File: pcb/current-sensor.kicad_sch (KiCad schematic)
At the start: 37 parts, among them U1 SS39ET, U2 TLV9064, U3 SS39ET

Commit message: Fixed part values; added name to scripts
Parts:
- C1, C10, C4, C5: LCSC C106217 -> C106857; MPN CC0603KRX7R8BB223 -> CC0603KRX7R8BB224; Mouser (none) -> 603-CC603KRX7R8BB224
- C11: Digikey (none) -> 1276-1870-2-ND; Mouser (none) -> 187-CL10A106MO8NQNC
- C3, C8, C9: Digikey (none) -> 1276-1005-2-ND; Mouser (none) -> 187-CL10B104KO8NNNC
- C7: Digikey (none) -> 311-4098-2-ND; Mouser (none) -> 603-CC603KRX7R9BB202
- R1, R5: Digikey (none) -> CR0603-JW-304ELFTR-ND; Mouser (none) -> 652-CR0603JW-304ELF
- R10, R11, R2, R8: Digikey (none) -> CR0603-JW-104ELFTR-ND; Mouser (none) -> 652-CR0603-JW-104ELF
- R3, R4, R9: Digikey (none) -> 541-4.99KHTR-ND; Mouser (none) -> 71-CRCW0603-4.99K-E3
- R6: Digikey (none) -> CR0603-JW-106ELFTR-ND; Mouser (none) -> 652-CR0603JW-106ELF
- R7: Digikey (none) -> CR0603-JW-105ELFTR-ND; Mouser (none) -> 652-CR0603JW-105ELF
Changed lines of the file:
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@@
 			)
 		)
+		(property "Digikey" "1276-1005-2-ND"
+			(at 128.27 55.88 0)
+			(effects
+				(font
+					(size 1.27 1.27)
+				)
+				(hide yes)
+			)
+		)
+		(property "Mouser" "187-CL10B104KO8NNNC"
+			(at 128.27 55.88 0)
+			(effects
+				(font
+					(size 1.27 1.27)
+				)
+				(hide yes)
+			)
+		)
 		(pin "1"
 		)
@@
 			)
 		)
-		(property "Digikey" ""
+		(property "Digikey" "CR0603-JW-104ELFTR-ND"
 			(at 38.1 163.83 90)
 			(effects
@@
 			)
 		)
-		(property "Mouser" ""
+		(property "Mouser" "652-CR0603-JW-104ELF"
 			(at 38.1 163.83 90)
 			(effects
@@
 			)
 		)
-		(property "MPN" "CC0603KRX7R8BB223"
+		(property "MPN" "CC0603KRX7R8BB224"
 			(at 162.56 71.12 0)
 			(effects
@@
 			)
 		)
-		(property "Mouser" ""
+		(property "Mouser" "603-CC603KRX7R8BB224"
 			(at 162.56 71.12 90)
 			(effects
@@
 			)
 		)
-		(property "LCSC" "C106217"
+		(property "LCSC" "C106857"
 			(at 162.56 71.12 0)
 			(effects
@@
 			)
 		)
+		(property "Digikey" "1276-1005-2-ND"
+			(at 107.95 154.94 0)
+			(effects
+				(font
+					(size 1.27 1.27)
+				)
+				(hide yes)
+			)
+		)
+		(property "Mouser" "187-CL10B104KO8NNNC"
+			(at 107.95 154.94 0)
+			(effects
+				(font
+					(size 1.27 1.27)
+				)
+				(hide yes)
+			)
+		)
 		(pin "1"
 		)
@@
 			)
 		)
-		(property "Digikey" ""
+		(property "Digikey" "541-4.99KHTR-ND"
 			(at 86.36 53.34 90)
 			(effects
@@
 			)
 		)
-		(property "Mouser" ""
+		(property "Mouser" "71-CRCW0603-4.99K-E3"
 			(at 86.36 53.34 90)
 			(effects
@@
 			)
 		)
-		(property "MPN" "CC0603KRX7R8BB223"
+		(property "MPN" "CC0603KRX7R8BB224"
 			(at 194.31 77.47 0)
 			(effects
@@
 			)
 		)
-		(property "Mouser" ""
+		(property "Mouser" "603-CC603KRX7R8BB224"
 			(at 194.31 77.47 90)
 			(effects
@@
 			)
 		)
-		(property "LCSC" "C106217"
+		(property "LCSC" "C106857"
 			(at 194.31 77.47 0)
 			(effects
@@
 			)
 		)
-		(property "Digikey" ""
+		(property "Digikey" "CR0603-JW-104ELFTR-ND"
 			(at 38.1 146.05 90)
 			(effects
@@
 			)
 		)
-		(property "Mouser" ""
+		(property "Mouser" "652-CR0603-JW-104ELF"
 			(at 38.1 146.05 90)
 			(effects
@@
 			)
 		)
-		(property "Digikey" ""
+		(property "Digikey" "541-4.99KHTR-ND"
 			(at 85.09 81.28 90)
 			(effects
@@
 			)
 		)
-		(property "Mouser" ""
+		(property "Mouser" "71-CRCW0603-4.99K-E3"
 			(at 85.09 81.28 90)
 			(effects
@@
 			)
 		)
-		(property "Digikey" ""
+		(property "Digikey" "CR0603-JW-106ELFTR-ND"
 			(at 199.39 77.47 90)
 			(effects
@@
 			)
 		)
-		(property "Mouser" ""
+		(property "Mouser" "652-CR0603JW-106ELF"
 			(at 199.39 77.47 90)
 			(effects
@@
 			)
 		)
-		(property "Mouser" ""
+		(property "Mouser" "603-CC603KRX7R9BB202"
 			(at 111.76 81.28 0)
 			(effects
@@
 			)
 		)
-		(property "Digikey" ""
+		(property "Digikey" "311-4098-2-ND"
 			(at 111.76 81.28 0)
 			(effects
@@
 			)
 		)
+		(property "Digikey" "1276-1005-2-ND"
+			(at 118.11 154.94 0)
+			(effects
+				(font
+					(size 1.27 1.27)
+				)
+				(hide yes)
+			)
+		)
+		(property "Mouser" "187-CL10B104KO8NNNC"
+			(at 118.11 154.94 0)
+			(effects
+				(font
+					(size 1.27 1.27)
+				)
+				(hide yes)
+			)
+		)
 		(pin "1"
 		)
@@
 			)
 		)
-		(property "Mouser" ""
+		(property "Mouser" "187-CL10A106MO8NQNC"
 			(at 30.48 163.83 0)
 			(effects
@@
 			)
 		)
-		(property "Digikey" ""
+		(property "Digikey" "1276-1870-2-ND"
 			(at 30.48 163.83 0)
 			(effects
@@
 			)
 		)
-		(property "Digikey" ""
+		(property "Digikey" "CR0603-JW-304ELFTR-ND"
 			(at 111.76 74.93 90)
 			(effects
@@
 			)
 		)
-		(property "Mouser" ""
+		(property "Mouser" "652-CR0603JW-304ELF"
 			(at 111.76 74.93 90)
 			(effects
@@
 			)
 		)
-		(property "Digikey" ""
+		(property "Digikey" "CR0603-JW-104ELFTR-ND"
 			(at 148.59 80.01 90)
 			(effects
@@
 			)
 		)
-		(property "Mouser" ""
+		(property "Mouser" "652-CR0603-JW-104ELF"
 			(at 148.59 80.01 90)
 			(effects
@@
 			)
 		)
-		(property "Digikey" ""
+		(property "Digikey" "CR0603-JW-304ELFTR-ND"
 			(at 85.09 35.56 90)
 			(effects
@@
 			)
 		)
-		(property "Mouser" ""
+		(property "Mouser" "652-CR0603JW-304ELF"
 			(at 85.09 35.56 90)
 			(effects
@@
 			)
 		)
-		(property "MPN" "CC0603KRX7R8BB223"
+		(property "MPN" "CC0603KRX7R8BB224"
 			(at 146.05 154.94 0)
 			(effects
@@
 			)
 		)
-		(property "Mouser" ""
+		(property "Mouser" "603-CC603KRX7R8BB224"
 			(at 146.05 154.94 90)
 			(effects
@@
 			)
 		)
-		(property "LCSC" "C106217"
+		(property "LCSC" "C106857"
 			(at 146.05 154.94 0)
 			(effects
@@
 			)
 		)
-		(property "Digikey" ""
+		(property "Digikey" "CR0603-JW-105ELFTR-ND"
 			(at 140.97 80.01 90)
 			(effects
@@
 			)
 		)
-		(property "Mouser" ""
+		(property "Mouser" "652-CR0603JW-105ELF"
 			(at 140.97 80.01 90)
 			(effects
@@
 			)
 		)
-		(property "Digikey" ""
+		(property "Digikey" "541-4.99KHTR-ND"
 			(at 187.96 58.42 90)
 			(effects
@@
 			)
 		)
-		(property "Mouser" ""
+		(property "Mouser" "71-CRCW0603-4.99K-E3"
 			(at 187.96 58.42 90)
 			(effects
@@
 			)
 		)
-		(property "MPN" "CC0603KRX7R8BB223"
+		(property "MPN" "CC0603KRX7R8BB224"
 			(at 208.28 41.91 0)
 			(effects
@@
 			)
 		)
-		(property "Mouser" ""
+		(property "Mouser" "603-CC603KRX7R8BB224"
 			(at 208.28 41.91 90)
 			(effects
@@
 			)
 		)
-		(property "LCSC" "C106217"
+		(property "LCSC" "C106857"
 			(at 208.28 41.91 0)
 			(effects
@@
 			)
 		)
-		(property "Digikey" ""
+		(property "Digikey" "CR0603-JW-104ELFTR-ND"
 			(at 201.93 35.56 90)
 			(effects
@@
 			)
 		)
-		(property "Mouser" ""
+		(property "Mouser" "652-CR0603-JW-104ELF"
 			(at 201.93 35.56 90)
 			(effects

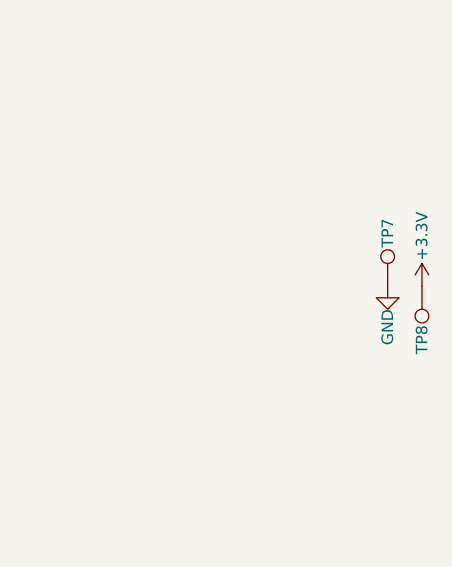
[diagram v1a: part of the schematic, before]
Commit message: Removed CSV bom file; moved logos to symbols
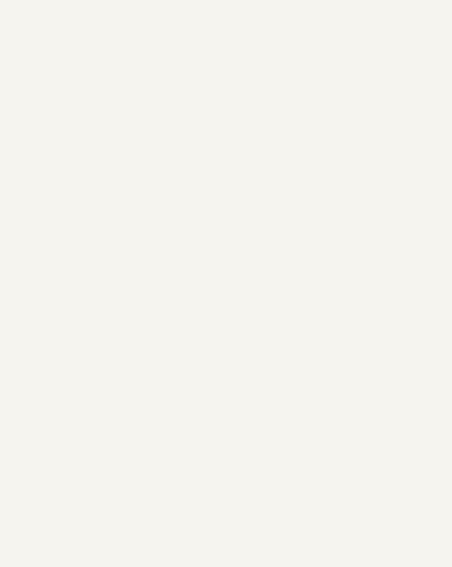
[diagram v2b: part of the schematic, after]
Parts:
- removed TP7, TP8: ~, CRGM Mechanical:TestPoint_Pad_D1.0mm, symbol Connector:TestPoint
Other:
- title: Current Detector -> Current Sensor

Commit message: Updated to all CRGM footprints
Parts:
- D1, D2: footprint Diode_SMD:D_SOD-323F -> CRGM Passive:D_SOD-323F
- U1, U3: footprint Package_TO_SOT_SMD:SOT-23 -> CRGM Passive:SOT-23
- U2: footprint Package_SO:SOIC-14_3.9x8.7mm_P1.27mm -> CRG Makes:SOIC-14_3.9x8.7mm_P1.27mm
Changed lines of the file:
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@@
 			)
 		)
-		(property "Footprint" "Package_SO:SOIC-14_3.9x8.7mm_P1.27mm"
+		(property "Footprint" "CRG Makes:SOIC-14_3.9x8.7mm_P1.27mm"
 			(at 162.56 55.88 0)
 			(effects
@@
 			)
 		)
-		(property "Footprint" "Package_TO_SOT_SMD:SOT-23"
+		(property "Footprint" "CRGM Passive:SOT-23"
 			(at 58.42 61.976 0)
 			(effects
@@
 			)
 		)
-		(property "Footprint" "Diode_SMD:D_SOD-323F"
+		(property "Footprint" "CRGM Passive:D_SOD-323F"
 			(at 130.175 80.01 0)
 			(effects
@@
 			)
 		)
-		(property "Footprint" "Package_SO:SOIC-14_3.9x8.7mm_P1.27mm"
+		(property "Footprint" "CRG Makes:SOIC-14_3.9x8.7mm_P1.27mm"
 			(at 55.88 153.67 0)
 			(effects
@@
 			)
 		)
-		(property "Footprint" "Diode_SMD:D_SOD-323F"
+		(property "Footprint" "CRGM Passive:D_SOD-323F"
 			(at 176.53 53.975 0)
 			(effects
@@
 			)
 		)
-		(property "Footprint" "Package_SO:SOIC-14_3.9x8.7mm_P1.27mm"
+		(property "Footprint" "CRG Makes:SOIC-14_3.9x8.7mm_P1.27mm"
 			(at 212.09 58.42 0)
 			(effects
@@
 			)
 		)
-		(property "Footprint" "Package_TO_SOT_SMD:SOT-23"
+		(property "Footprint" "CRGM Passive:SOT-23"
 			(at 58.42 89.916 0)
 			(effects
@@
 			)
 		)
-		(property "Footprint" "Package_SO:SOIC-14_3.9x8.7mm_P1.27mm"
+		(property "Footprint" "CRG Makes:SOIC-14_3.9x8.7mm_P1.27mm"
 			(at 109.22 53.34 0)
 			(effects
@@
 			)
 		)
-		(property "Footprint" "Package_SO:SOIC-14_3.9x8.7mm_P1.27mm"
+		(property "Footprint" "CRG Makes:SOIC-14_3.9x8.7mm_P1.27mm"
 			(at 109.22 53.34 0)
 			(effects

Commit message: Updated part properties for consistency
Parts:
- C1, C10, C11, C2, C3, C4, C5, C6, C8, C9: Tolerance (none) -> 10%
- R1, R10, R11, R2, R5, R6, R7, R8: Tolerance (none) -> 5%
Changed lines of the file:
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@@
 			)
 		)
+		(property "Tolerance" "10%"
+			(at 128.27 55.88 90)
+			(effects
+				(font
+					(size 1.27 1.27)
+				)
+				(hide yes)
+			)
+		)
 		(pin "1"
 		)
@@
 			)
 		)
+		(property "Tolerance" "10%"
+			(at 77.47 81.28 90)
+			(effects
+				(font
+					(size 1.27 1.27)
+				)
+				(hide yes)
+			)
+		)
 		(pin "1"
 		)
@@
 			)
 		)
+		(property "Tolerance" "5%"
+			(at 38.1 163.83 90)
+			(effects
+				(font
+					(size 1.27 1.27)
+				)
+				(hide yes)
+			)
+		)
 		(pin "2"
 		)
@@
 			)
 		)
+		(property "Tolerance" "10%"
+			(at 162.56 71.12 90)
+			(effects
+				(font
+					(size 1.27 1.27)
+				)
+				(hide yes)
+			)
+		)
 		(pin "1"
 		)
@@
 			)
 		)
+		(property "Tolerance" "10%"
+			(at 107.95 154.94 0)
+			(effects
+				(font
+					(size 1.27 1.27)
+				)
+				(hide yes)
+			)
+		)
 		(pin "1"
 		)
@@
 			)
 		)
+		(property "Tolerance" "10%"
+			(at 194.31 77.47 90)
+			(effects
+				(font
+					(size 1.27 1.27)
+				)
+				(hide yes)
+			)
+		)
 		(pin "1"
 		)
@@
 			)
 		)
+		(property "Tolerance" "5%"
+			(at 38.1 146.05 90)
+			(effects
+				(font
+					(size 1.27 1.27)
+				)
+				(hide yes)
+			)
+		)
 		(pin "2"
 		)
@@
 			)
 		)
+		(property "Tolerance" "5%"
+			(at 199.39 77.47 90)
+			(effects
+				(font
+					(size 1.27 1.27)
+				)
+				(hide yes)
+			)
+		)
 		(pin "2"
 		)
@@
 			)
 		)
+		(property "Tolerance" "10%"
+			(at 118.11 154.94 0)
+			(effects
+				(font
+					(size 1.27 1.27)
+				)
+				(hide yes)
+			)
+		)
 		(pin "1"
 		)
@@
 			)
 		)
+		(property "Tolerance" "10%"
+			(at 30.48 163.83 0)
+			(effects
+				(font
+					(size 1.27 1.27)
+				)
+				(hide yes)
+			)
+		)
 		(pin "1"
 		)
@@
 			)
 		)
+		(property "Tolerance" "5%"
+			(at 111.76 74.93 90)
+			(effects
+				(font
+					(size 1.27 1.27)
+				)
+				(hide yes)
+			)
+		)
 		(pin "2"
 		)
@@
 			)
 		)
+		(property "Tolerance" "5%"
+			(at 148.59 80.01 90)
+			(effects
+				(font
+					(size 1.27 1.27)
+				)
+				(hide yes)
+			)
+		)
 		(pin "2"
 		)
@@
 			)
 		)
+		(property "Tolerance" "5%"
+			(at 85.09 35.56 90)
+			(effects
+				(font
+					(size 1.27 1.27)
+				)
+				(hide yes)
+			)
+		)
 		(pin "2"
 		)
@@
 			)
 		)
+		(property "Tolerance" "10%"
+			(at 146.05 154.94 90)
+			(effects
+				(font
+					(size 1.27 1.27)
+				)
+				(hide yes)
+			)
+		)
 		(pin "1"
 		)
@@
 			)
 		)
+		(property "Tolerance" "5%"
+			(at 140.97 80.01 90)
+			(effects
+				(font
+					(size 1.27 1.27)
+				)
+				(hide yes)
+			)
+		)
 		(pin "2"
 		)
@@
 			)
 		)
+		(property "Tolerance" "10%"
+			(at 78.74 53.34 90)
+			(effects
+				(font
+					(size 1.27 1.27)
+				)
+				(hide yes)
+			)
+		)
 		(pin "1"
 		)
@@
 			)
 		)
+		(property "Tolerance" "10%"
+			(at 208.28 41.91 90)
+			(effects
+				(font
+					(size 1.27 1.27)
+				)
+				(hide yes)
+			)
+		)
 		(pin "1"
 		)
@@
 			(at 201.93 35.56 90)
 			(effects
+				(font
+					(size 1.27 1.27)
+				)
+				(hide yes)
+			)
+		)
+		(property "Tolerance" "5%"
+			(at 201.93 35.56 90)
+			(effects

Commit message: Redesign with MCU
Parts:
- removed J1: ~, CRGM Connector:JST_SH_SM03B-SRSS-TB_1x03-1MP_P1.00mm_Horizontal, symbol CRGM Connector:JST-SH-3

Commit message: Clean up, arranging, ERC and DCR
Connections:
- net PEAK: now reaches C3.2, D2.1 (K), R7.1, TP2.1, U2.12 (+)
- net H2IN: now reaches C6.2, R9.2
- net DCBIAS: now reaches R1.1, R3.1, TP1.1, U2.3 (+)
- net H1IN: now reaches C2.2, R3.2
- net GAIN: now reaches C5.2, R4.1, R6.1, TP3.1, U2.10 (+)
- net LOWPASS: now reaches C7.1, R5.2, R9.1, TP5.1, U2.2 (-)
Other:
- moved on the sheet: C2, C6, U1, U3

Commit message: Fixed LCSC part numbers and attributes
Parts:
- C7: Tolerance (none) -> 10%
- RV1: Tolerance (none) -> 25%
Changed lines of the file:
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@@
+			)
+		)
+		(property "Tolerance" "25%"
+			(at 214.63 35.56 90)
+			(effects
+				(font
+					(size 1.27 1.27)
+				)
+				(hide yes)
 			)
 		)
@@
 			(effects
 				(font
+					(size 1.27 1.27)
+				)
+				(hide yes)
+			)
+		)
+		(property "Tolerance" "10%"
+			(at 111.76 81.28 90)
+			(effects
+				(font

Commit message: Updated part for availability and price
Adjusted origin.
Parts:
- C1, C10, C4, C5: LCSC C106857 -> C106249; MPN CC0603KRX7R8BB224 -> CC0603KRX7R7BB224
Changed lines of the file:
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@@
 			)
 		)
-		(property "Description" "50V 220nF X7R ±10% 0603 Multilayer Ceramic Capacitors MLCC"
+		(property "Description" "16V 220nF X7R ±10% 0603 Multilayer Ceramic Capacitors MLCC"
 			(at 162.56 71.12 0)
 			(effects
@@
 			)
 		)
-		(property "MPN" "CC0603KRX7R8BB224"
+		(property "MPN" "CC0603KRX7R7BB224"
 			(at 162.56 71.12 0)
 			(effects
@@
 			)
 		)
-		(property "LCSC" "C106857"
+		(property "LCSC" "C106249"
 			(at 162.56 71.12 0)
 			(effects
@@
 			)
 		)
-		(property "Description" "50V 220nF X7R ±10% 0603 Multilayer Ceramic Capacitors MLCC"
+		(property "Description" "16V 220nF X7R ±10% 0603 Multilayer Ceramic Capacitors MLCC"
 			(at 194.31 77.47 0)
 			(effects
@@
 			)
 		)
-		(property "MPN" "CC0603KRX7R8BB224"
+		(property "MPN" "CC0603KRX7R7BB224"
 			(at 194.31 77.47 0)
 			(effects
@@
 			)
 		)
-		(property "LCSC" "C106857"
+		(property "LCSC" "C106249"
 			(at 194.31 77.47 0)
 			(effects
@@
 			)
 		)
-		(property "Description" "50V 220nF X7R ±10% 0603 Multilayer Ceramic Capacitors MLCC"
+		(property "Description" "16V 220nF X7R ±10% 0603 Multilayer Ceramic Capacitors MLCC"
 			(at 146.05 154.94 0)
 			(effects
@@
 			)
 		)
-		(property "MPN" "CC0603KRX7R8BB224"
+		(property "MPN" "CC0603KRX7R7BB224"
 			(at 146.05 154.94 0)
 			(effects
@@
 			)
 		)
-		(property "LCSC" "C106857"
+		(property "LCSC" "C106249"
 			(at 146.05 154.94 0)
 			(effects
@@
 			)
 		)
-		(property "Description" "50V 220nF X7R ±10% 0603 Multilayer Ceramic Capacitors MLCC"
+		(property "Description" "16V 220nF X7R ±10% 0603 Multilayer Ceramic Capacitors MLCC"
 			(at 208.28 41.91 0)
 			(effects
@@
 			)
 		)
-		(property "MPN" "CC0603KRX7R8BB224"
+		(property "MPN" "CC0603KRX7R7BB224"
 			(at 208.28 41.91 0)
 			(effects
@@
 			)
 		)
-		(property "LCSC" "C106857"
+		(property "LCSC" "C106249"
 			(at 208.28 41.91 0)
 			(effects
